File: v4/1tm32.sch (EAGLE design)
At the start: 50 parts, among them IC1 STM32L412RBT6P, J2 10118192-0001LF, SW1 LL3301FF065QJ, U2 LD39050PU33R, Y1 8MHz, Y2 32.7KHz

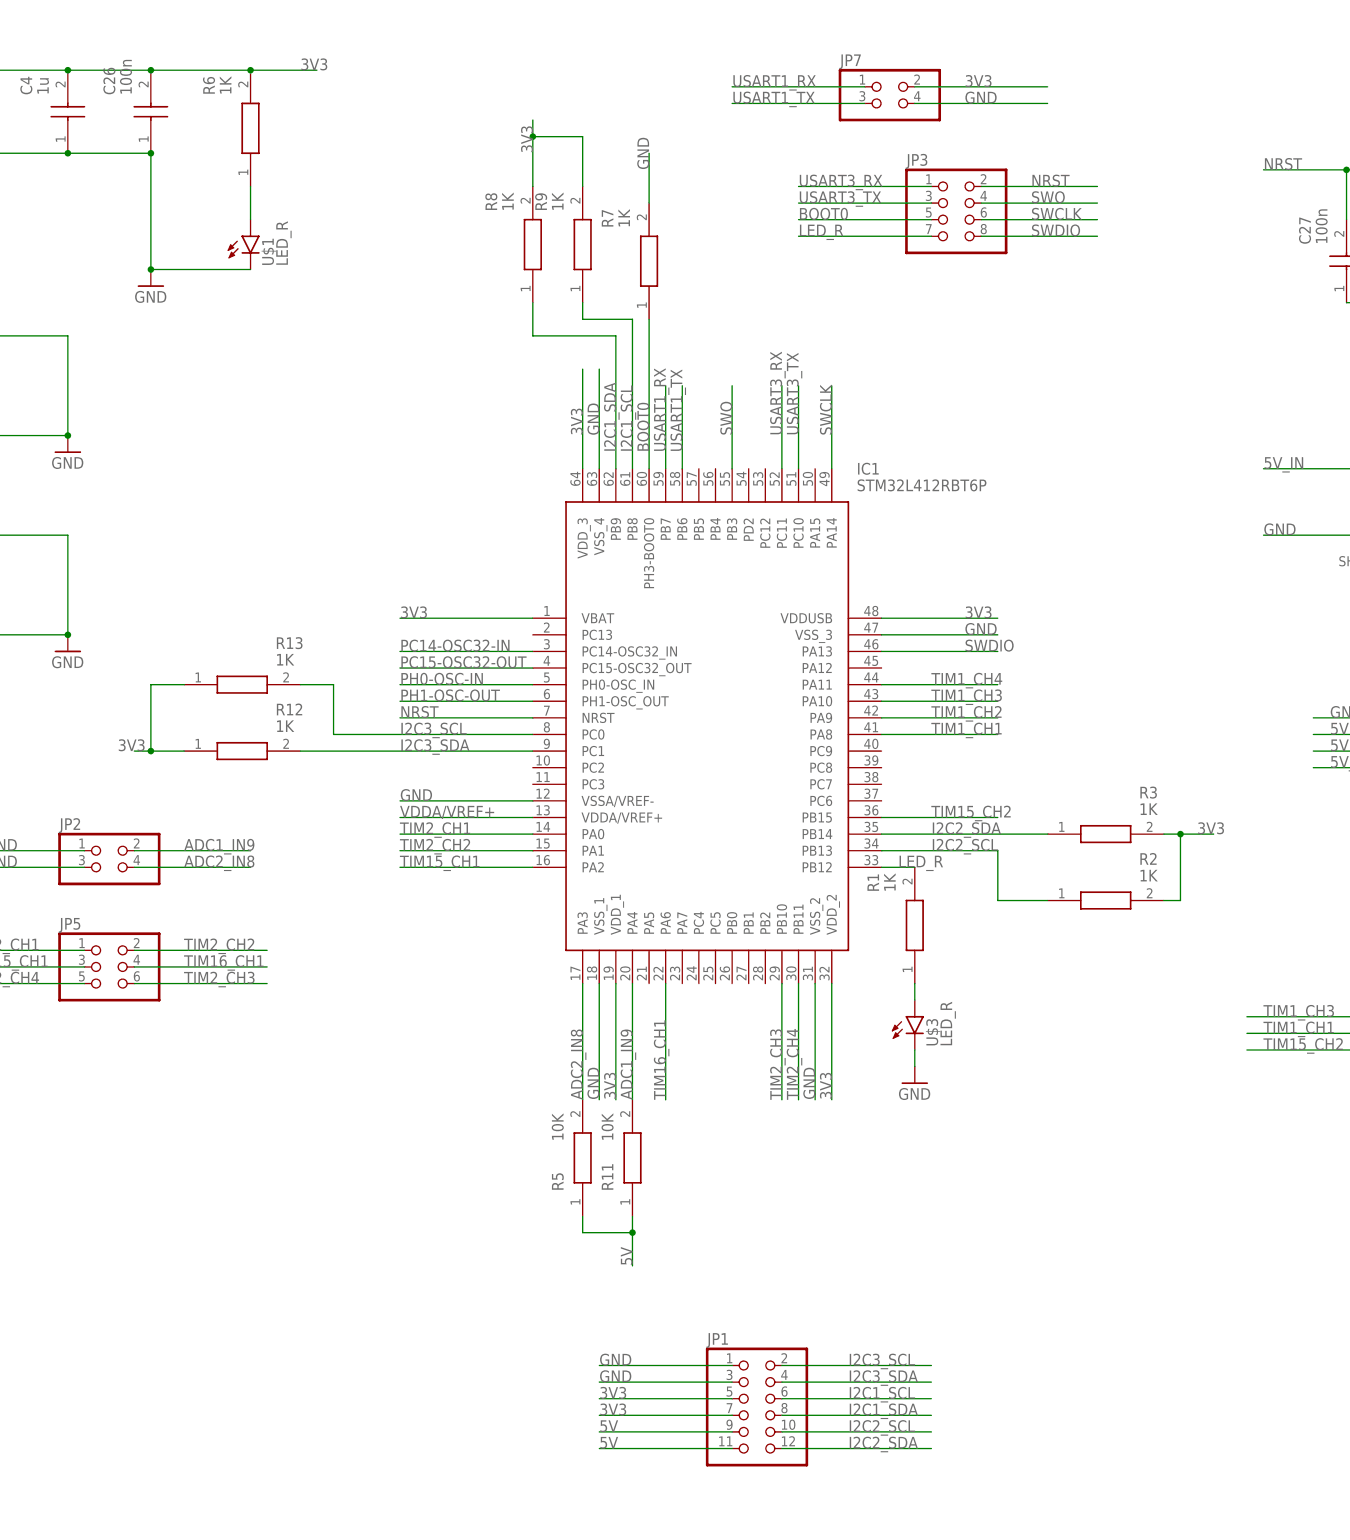
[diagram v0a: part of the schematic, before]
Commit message: modified i2c headers
removed resistors
changed 3v3 pins to gpio pins
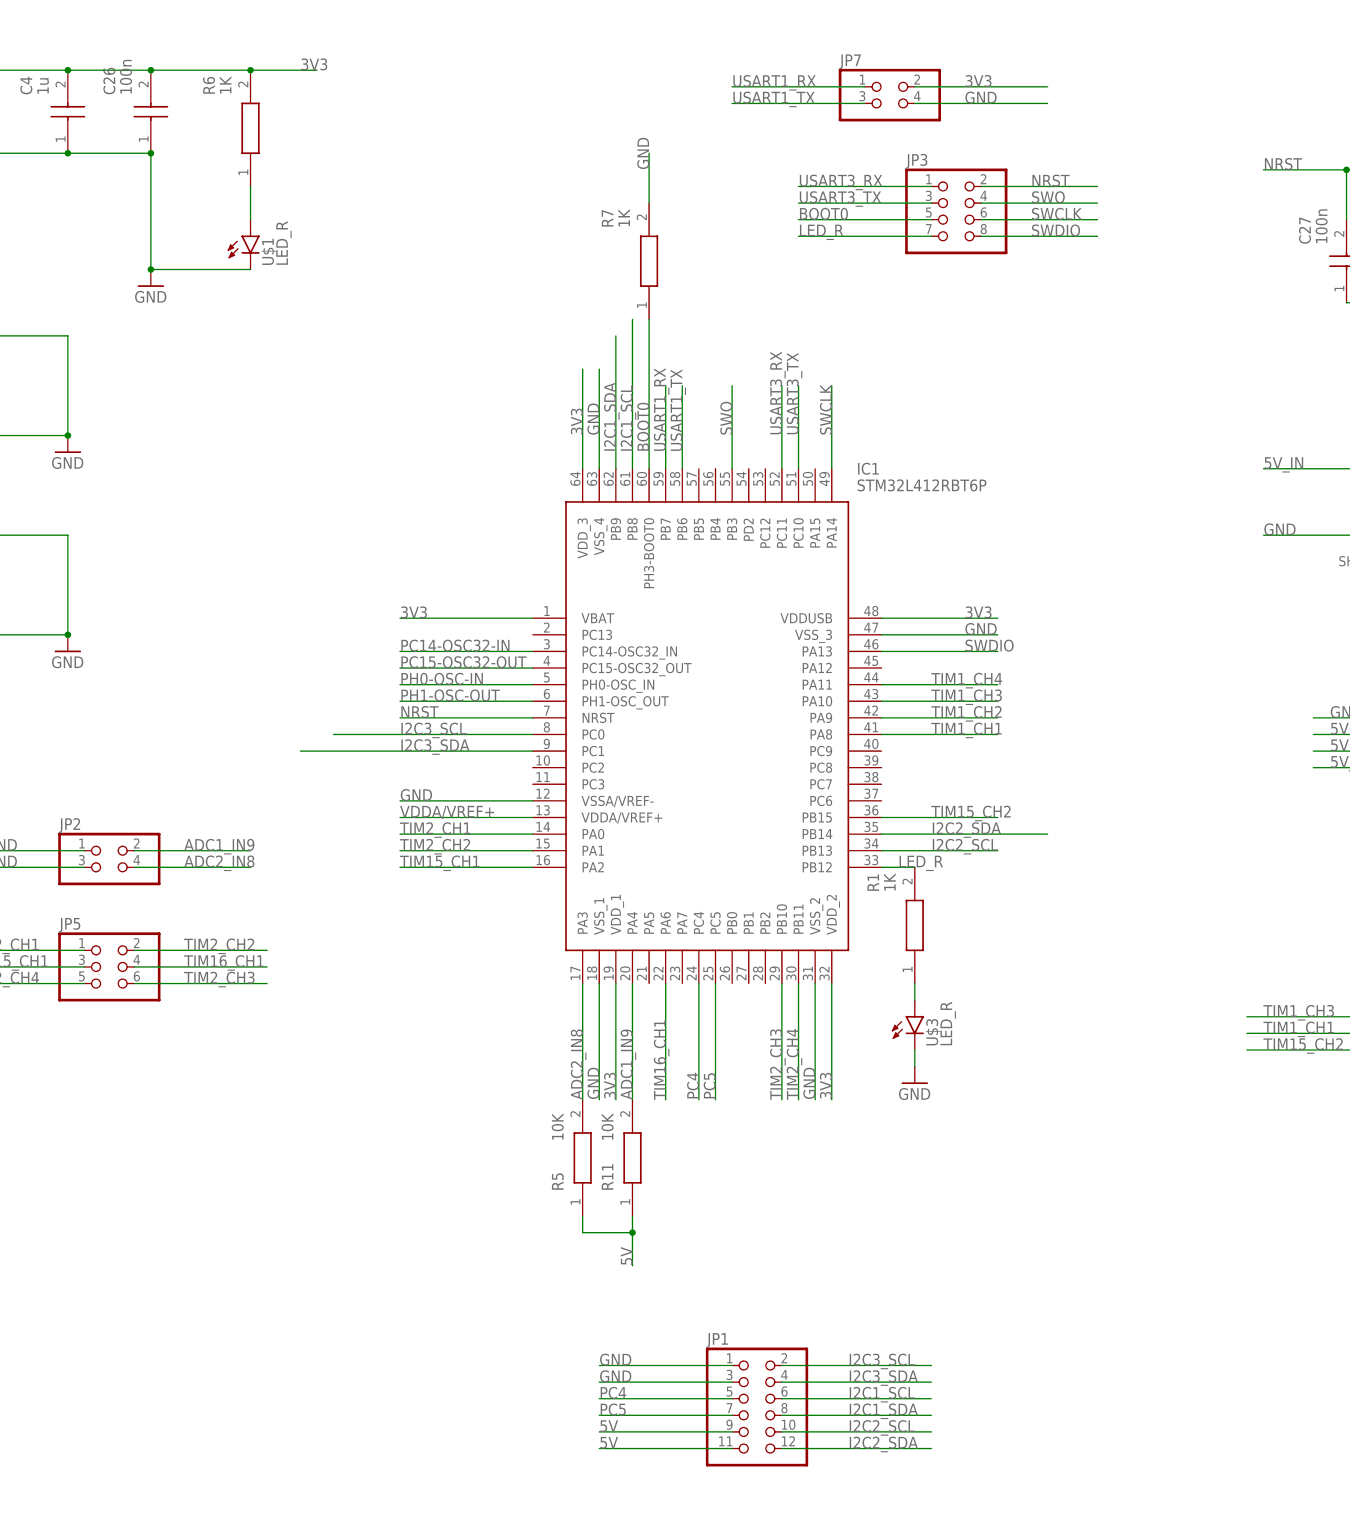
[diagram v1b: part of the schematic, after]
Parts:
- removed R12, R13, R2, R3, R8, R9: 1K, RC0805FR-131KL:RC0805FR-131KL
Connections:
- new net PC4: IC1.PC4, JP1.5
- new net PC5: IC1.PC5, JP1.7
- net 3V3: no longer JP1.5, JP1.7, R12.1, R13.1, R2.2, R3.2, R8.2, R9.2
- net I2C1_SCL: no longer R9.1
- net I2C1_SDA: no longer R8.1
- net I2C2_SCL: no longer R2.1
- net I2C2_SDA: no longer R3.1
- net I2C3_SCL: no longer R13.2
- net I2C3_SDA: no longer R12.2
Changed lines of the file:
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@@
 <part name="R6" library="RC0805FR-131KL" deviceset="RC0805FR-131KL" device="" value="1K"/>
 <part name="R7" library="RC0805FR-131KL" deviceset="RC0805FR-131KL" device="" value="1K"/>
-<part name="R8" library="RC0805FR-131KL" deviceset="RC0805FR-131KL" device="" value="1K"/>
-<part name="R9" library="RC0805FR-131KL" deviceset="RC0805FR-131KL" device="" value="1K"/>
 <part name="R10" library="RC0805JR-0710KL" deviceset="RC0805JR-0710KL" device="" value="10K"/>
 <part name="R1" library="RC0805FR-131KL" deviceset="RC0805FR-131KL" device="" value="1K"/>
@@
 <part name="R11" library="RC0805JR-0710KL" deviceset="RC0805JR-0710KL" device="" value="10K"/>
 <part name="U$2" library="RBR1L30ATE25(scho_diode)" deviceset="RBR1L30ATE25" device=""/>
-<part name="R2" library="RC0805FR-131KL" deviceset="RC0805FR-131KL" device="" value="1K"/>
-<part name="R3" library="RC0805FR-131KL" deviceset="RC0805FR-131KL" device="" value="1K"/>
-<part name="R12" library="RC0805FR-131KL" deviceset="RC0805FR-131KL" device="" value="1K"/>
-<part name="R13" library="RC0805FR-131KL" deviceset="RC0805FR-131KL" device="" value="1K"/>
 <part name="JP1" library="pinhead" library_urn="urn:adsk.eagle:library:325" deviceset="PINHD-2X6" device="" package3d_urn="urn:adsk.eagle:package:22474/2"/>
 <part name="JP2" library="pinhead" library_urn="urn:adsk.eagle:library:325" deviceset="PINHD-2X2" device="" package3d_urn="urn:adsk.eagle:package:22455/2"/>
@@
 <attribute name="VALUE" x="29.21" y="107.95" size="1.778" layer="96" rot="R90" align="center-left"/>
 </instance>
-<instance part="R8" gate="G$1" x="15.24" y="96.52" smashed="yes" rot="R90">
-<attribute name="NAME" x="8.89" y="110.49" size="1.778" layer="95" rot="R90" align="center-left"/>
-<attribute name="VALUE" x="11.43" y="110.49" size="1.778" layer="96" rot="R90" align="center-left"/>
-</instance>
-<instance part="R9" gate="G$1" x="22.86" y="96.52" smashed="yes" rot="R90">
-<attribute name="NAME" x="16.51" y="110.49" size="1.778" layer="95" rot="R90" align="center-left"/>
-<attribute name="VALUE" x="19.05" y="110.49" size="1.778" layer="96" rot="R90" align="center-left"/>
-</instance>
 <instance part="R10" gate="G$1" x="162.56" y="116.84" smashed="yes" rot="R90">
 <attribute name="NAME" x="156.21" y="130.81" size="1.778" layer="95" rot="R90" align="center-left"/>
@@
 <attribute name="NAME" x="-142.5956" y="122.9614" size="2.0828" layer="95" ratio="6" rot="SR180"/>
 <attribute name="VALUE" x="-141.9606" y="125.5014" size="2.0828" layer="96" ratio="6" rot="SR180"/>
-</instance>
-<instance part="R2" gate="G$1" x="93.98" y="5.08" smashed="yes">
-<attribute name="NAME" x="107.95" y="11.43" size="1.778" layer="95" align="center-left"/>
-<attribute name="VALUE" x="107.95" y="8.89" size="1.778" layer="96" align="center-left"/>
-</instance>
-<instance part="R3" gate="G$1" x="93.98" y="15.24" smashed="yes">
-<attribute name="NAME" x="107.95" y="21.59" size="1.778" layer="95" align="center-left"/>
-<attribute name="VALUE" x="107.95" y="19.05" size="1.778" layer="96" align="center-left"/>
-</instance>
-<instance part="R12" gate="G$1" x="-38.1" y="27.94" smashed="yes">
-<attribute name="NAME" x="-24.13" y="34.29" size="1.778" layer="95" align="center-left"/>
-<attribute name="VALUE" x="-24.13" y="31.75" size="1.778" layer="96" align="center-left"/>
-</instance>
-<instance part="R13" gate="G$1" x="-38.1" y="38.1" smashed="yes">
-<attribute name="NAME" x="-24.13" y="44.45" size="1.778" layer="95" align="center-left"/>
-<attribute name="VALUE" x="-24.13" y="41.91" size="1.778" layer="96" align="center-left"/>
 </instance>
 <instance part="JP1" gate="A" x="48.26" y="-71.12" smashed="yes">
@@
 <net name="I2C1_SDA" class="0">
 <segment>
-<pinref part="R8" gate="G$1" pin="1"/>
-<wire x1="15.24" y1="96.52" x2="15.24" y2="91.44" width="0.1524" layer="91"/>
-<wire x1="15.24" y1="91.44" x2="27.94" y2="91.44" width="0.1524" layer="91"/>
 <pinref part="IC1" gate="G$1" pin="PB9"/>
 <wire x1="27.94" y1="91.44" x2="27.94" y2="71.12" width="0.1524" layer="91"/>
@@
 <net name="I2C1_SCL" class="0">
 <segment>
-<pinref part="R9" gate="G$1" pin="1"/>
-<wire x1="22.86" y1="96.52" x2="22.86" y2="93.98" width="0.1524" layer="91"/>
 <pinref part="IC1" gate="G$1" pin="PB8"/>
-<wire x1="22.86" y1="93.98" x2="30.48" y2="93.98" width="0.1524" layer="91"/>
 <wire x1="30.48" y1="93.98" x2="30.48" y2="71.12" width="0.1524" layer="91"/>
 <label x="30.48" y="73.66" size="1.778" layer="95" rot="R90"/>
@@
 </segment>
 <segment>
-<wire x1="15.24" y1="114.3" x2="15.24" y2="121.92" width="0.1524" layer="91"/>
-<wire x1="15.24" y1="121.92" x2="15.24" y2="124.46" width="0.1524" layer="91"/>
-<wire x1="22.86" y1="114.3" x2="22.86" y2="121.92" width="0.1524" layer="91"/>
-<wire x1="22.86" y1="121.92" x2="15.24" y2="121.92" width="0.1524" layer="91"/>
-<junction x="15.24" y="121.92"/>
-<label x="15.24" y="119.38" size="1.778" layer="95" rot="R90"/>
-<pinref part="R8" gate="G$1" pin="2"/>
-<pinref part="R9" gate="G$1" pin="2"/>
-</segment>
-<segment>
-<pinref part="R3" gate="G$1" pin="2"/>
-<wire x1="111.76" y1="15.24" x2="114.3" y2="15.24" width="0.1524" layer="91"/>
-<pinref part="R2" gate="G$1" pin="2"/>
-<wire x1="114.3" y1="15.24" x2="119.38" y2="15.24" width="0.1524" layer="91"/>
-<wire x1="111.76" y1="5.08" x2="114.3" y2="5.08" width="0.1524" layer="91"/>
-<wire x1="114.3" y1="5.08" x2="114.3" y2="15.24" width="0.1524" layer="91"/>
-<junction x="114.3" y="15.24"/>
-<label x="116.84" y="15.24" size="1.778" layer="95"/>
-</segment>
-<segment>
-<pinref part="R12" gate="G$1" pin="1"/>
-<wire x1="-38.1" y1="27.94" x2="-43.18" y2="27.94" width="0.1524" layer="91"/>
-<pinref part="R13" gate="G$1" pin="1"/>
-<wire x1="-43.18" y1="27.94" x2="-45.72" y2="27.94" width="0.1524" layer="91"/>
-<wire x1="-38.1" y1="38.1" x2="-43.18" y2="38.1" width="0.1524" layer="91"/>
-<wire x1="-43.18" y1="38.1" x2="-43.18" y2="27.94" width="0.1524" layer="91"/>
-<junction x="-43.18" y="27.94"/>
-<label x="-48.26" y="27.94" size="1.778" layer="95"/>
-</segment>
-<segment>
-<pinref part="JP1" gate="A" pin="5"/>
-<wire x1="45.72" y1="-71.12" x2="25.4" y2="-71.12" width="0.1524" layer="91"/>
-<label x="25.4" y="-71.12" size="1.778" layer="95"/>
-</segment>
-<segment>
-<pinref part="JP1" gate="A" pin="7"/>
-<wire x1="45.72" y1="-73.66" x2="25.4" y2="-73.66" width="0.1524" layer="91"/>
-<label x="25.4" y="-73.66" size="1.778" layer="95"/>
-</segment>
-<segment>
 <pinref part="JP7" gate="A" pin="2"/>
 <wire x1="73.66" y1="129.54" x2="93.98" y2="129.54" width="0.1524" layer="91"/>
@@
 <wire x1="68.58" y1="12.7" x2="86.36" y2="12.7" width="0.1524" layer="91"/>
 <label x="76.2" y="12.7" size="1.778" layer="95"/>
-<pinref part="R2" gate="G$1" pin="1"/>
-<wire x1="86.36" y1="12.7" x2="86.36" y2="5.08" width="0.1524" layer="91"/>
-<wire x1="86.36" y1="5.08" x2="93.98" y2="5.08" width="0.1524" layer="91"/>
 </segment>
 <segment>
@@
 <wire x1="68.58" y1="15.24" x2="93.98" y2="15.24" width="0.1524" layer="91"/>
 <label x="76.2" y="15.24" size="1.778" layer="95"/>
-<pinref part="R3" gate="G$1" pin="1"/>
 </segment>
 <segment>
@@
 <wire x1="15.24" y1="30.48" x2="-15.24" y2="30.48" width="0.1524" layer="91"/>
 <label x="-5.08" y="30.48" size="1.778" layer="95"/>
-<wire x1="-15.24" y1="30.48" x2="-15.24" y2="38.1" width="0.1524" layer="91"/>
-<pinref part="R13" gate="G$1" pin="2"/>
-<wire x1="-15.24" y1="38.1" x2="-20.32" y2="38.1" width="0.1524" layer="91"/>
 </segment>
 <segment>
@@
 <wire x1="15.24" y1="27.94" x2="-20.32" y2="27.94" width="0.1524" layer="91"/>
 <label x="-5.08" y="27.94" size="1.778" layer="95"/>
-<pinref part="R12" gate="G$1" pin="2"/>
 </segment>
 <segment>
@@
 </segment>
 </net>
+<net name="PC4" class="0">
+<segment>
+<pinref part="IC1" gate="G$1" pin="PC4"/>
+<wire x1="40.64" y1="-7.62" x2="40.64" y2="-25.4" width="0.1524" layer="91"/>
+<label x="40.64" y="-25.4" size="1.778" layer="95" rot="R90"/>
+</segment>
+<segment>
+<pinref part="JP1" gate="A" pin="5"/>
+<wire x1="45.72" y1="-71.12" x2="25.4" y2="-71.12" width="0.1524" layer="91"/>
+<label x="25.4" y="-71.12" size="1.778" layer="95"/>
+</segment>
+</net>
+<net name="PC5" class="0">
+<segment>
+<pinref part="IC1" gate="G$1" pin="PC5"/>
+<wire x1="43.18" y1="-7.62" x2="43.18" y2="-25.4" width="0.1524" layer="91"/>
+<label x="43.18" y="-25.4" size="1.778" layer="95" rot="R90"/>
+</segment>
+<segment>
+<pinref part="JP1" gate="A" pin="7"/>
+<wire x1="45.72" y1="-73.66" x2="25.4" y2="-73.66" width="0.1524" layer="91"/>
+<label x="25.4" y="-73.66" size="1.778" layer="95"/>
+</segment>
+</net>

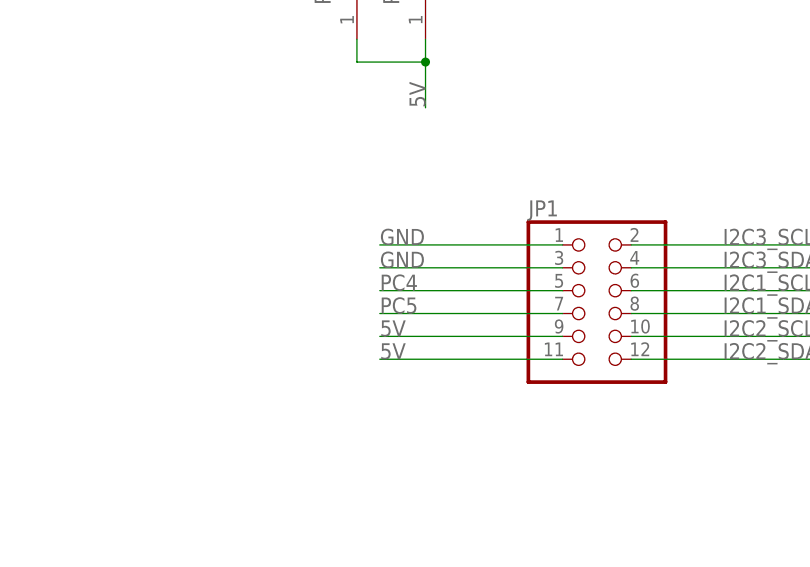
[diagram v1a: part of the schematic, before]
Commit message: moved wire around to space for pwm wave
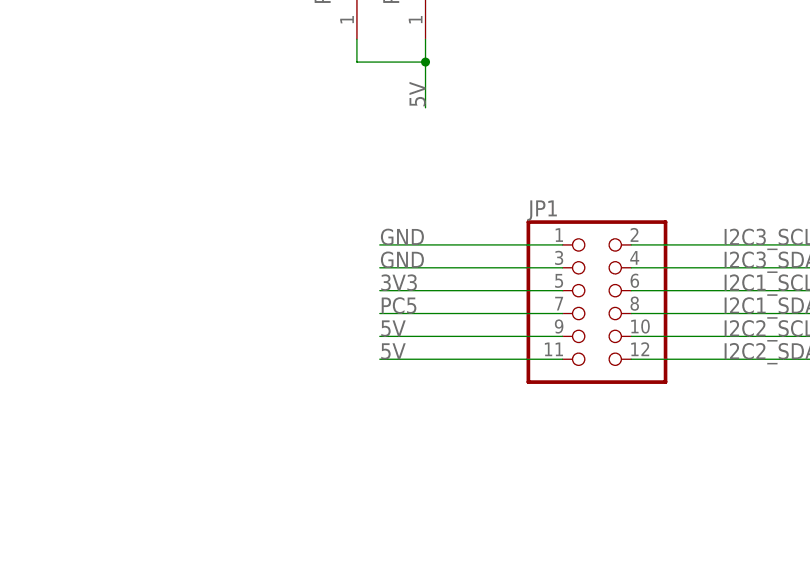
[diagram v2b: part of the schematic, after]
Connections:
- net 3V3: now also JP1.5
- net PC4: no longer JP1.5
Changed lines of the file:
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@@
 <label x="165.1" y="25.4" size="1.778" layer="95"/>
+</segment>
+<segment>
+<pinref part="JP1" gate="A" pin="5"/>
+<wire x1="45.72" y1="-71.12" x2="25.4" y2="-71.12" width="0.1524" layer="91"/>
+<label x="25.4" y="-71.12" size="1.778" layer="95"/>
 </segment>
 </net>
@@
 <label x="40.64" y="-25.4" size="1.778" layer="95" rot="R90"/>
 </segment>
-<segment>
-<pinref part="JP1" gate="A" pin="5"/>
-<wire x1="45.72" y1="-71.12" x2="25.4" y2="-71.12" width="0.1524" layer="91"/>
-<label x="25.4" y="-71.12" size="1.778" layer="95"/>
-</segment>
-</net>
+</net>
